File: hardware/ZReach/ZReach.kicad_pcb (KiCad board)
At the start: 4 copper layers, 120 x 120 mm, 54 parts, among them J1 USB_C_Receptacle_USB2.0, J2 Conn_02x05_Odd_Even, J3 SMA, J4 NM, J5 Qwiic_RA, J6 Conn_01x02, J7 Conn_01x05, J8 Conn_01x05, SW1 PTS810, U1 CP2102N-Axx-xQFN20, U2 EFR32xG23-QFN48, U3 AP2127K-3.3, Y1 39MHz 10ppm, Y2 32768Hz

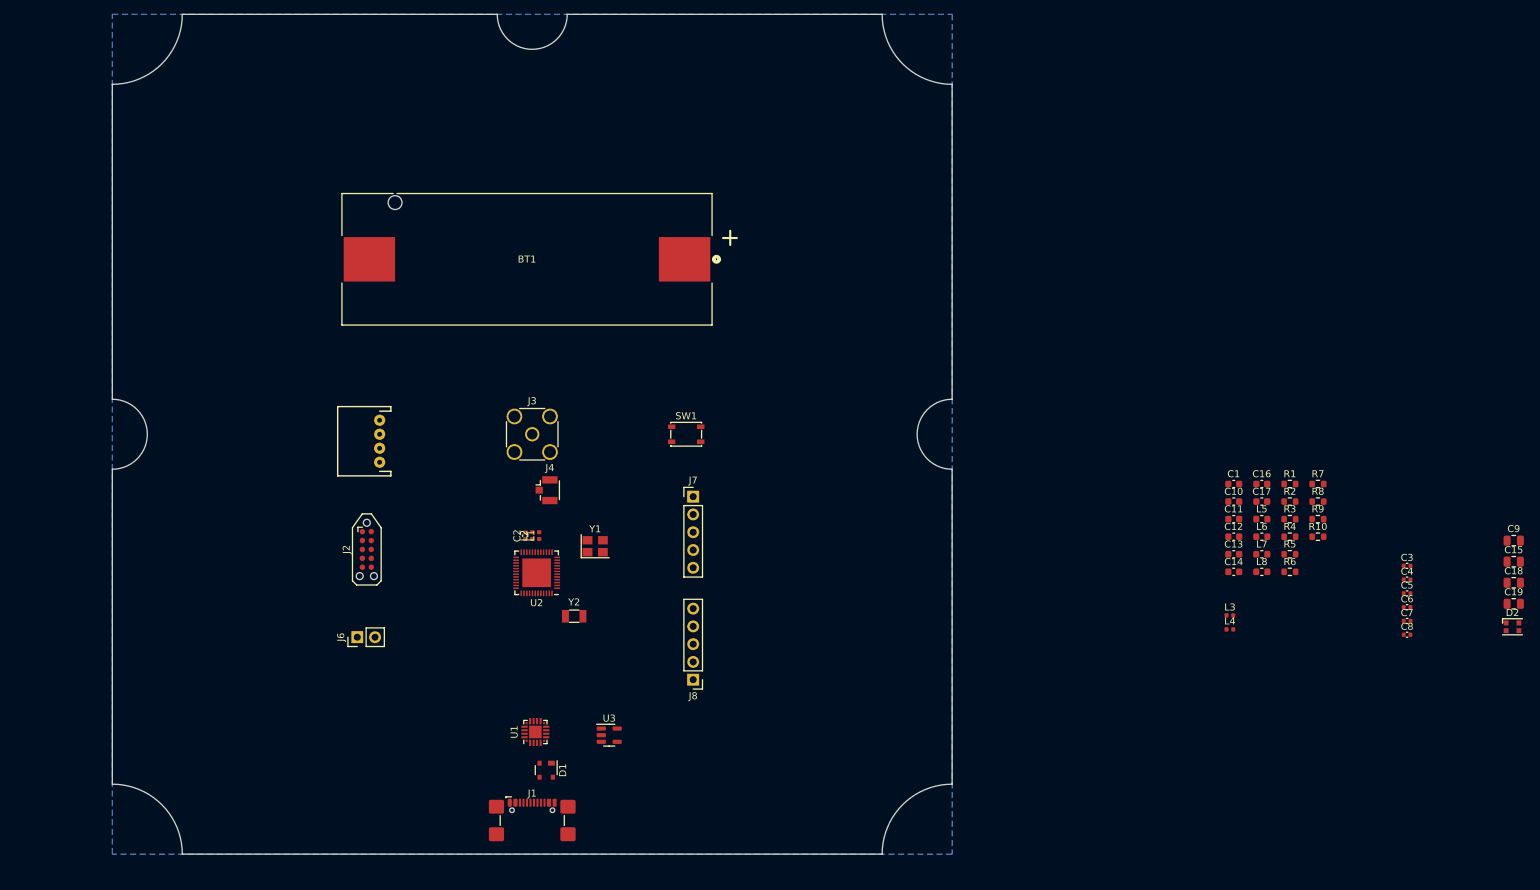
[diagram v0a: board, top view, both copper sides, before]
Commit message: PCB Layout DRC clean but needs more cleanup
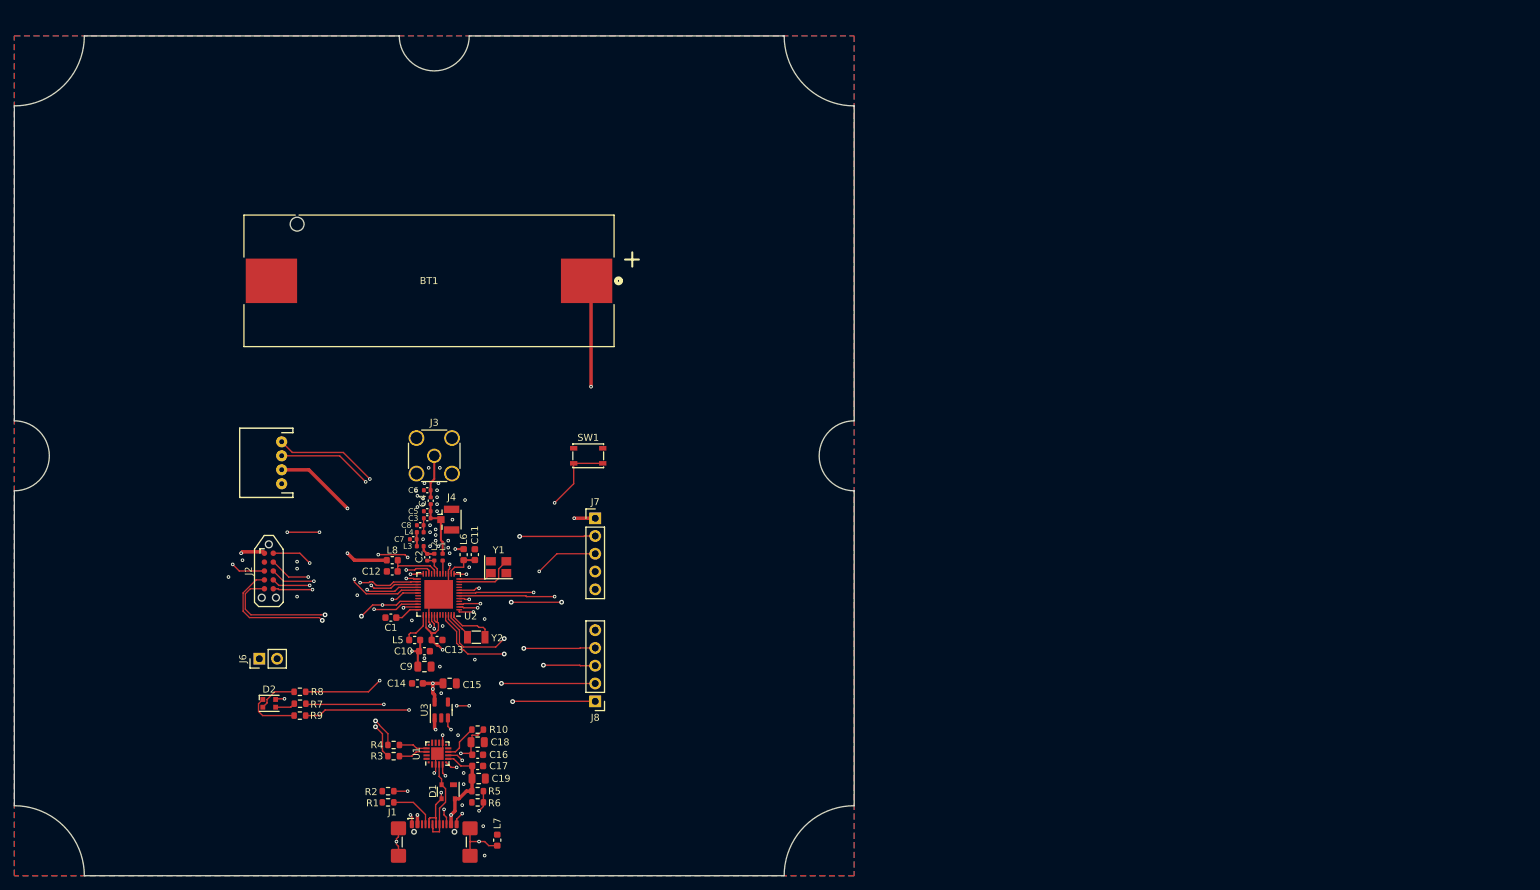
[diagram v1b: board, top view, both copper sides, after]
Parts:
- moved D2 178.0 mm to (177.4, 123.5)
- moved C9 156.7 mm to (199.6, 118.2), turned to 180 degrees
- moved C15 153.0 mm to (203.2, 120.6), turned to 180 degrees
- moved C19 150.0 mm to (207.3, 134.2), turned to 180 degrees
- moved C18 149.8 mm to (207.2, 129.0), turned to 180 degrees
- moved R7 148.8 mm to (181.8, 123.5)
- moved R9 148.2 mm to (181.8, 125.2)
- moved R8 148.0 mm to (181.8, 121.8)
- moved C7 142.5 mm to (198.0, 100.0), turned to 180 degrees
- moved C8 141.9 mm to (199.0, 98.0), turned to 180 degrees
- moved C6 141.0 mm to (200.0, 93.0)
- moved C5 140.5 mm to (200.0, 96.0)
- moved C3 140.2 mm to (200.0, 97.0)
- moved C4 140.0 mm to (200.5, 94.5), turned to 90 degrees
- moved R1 136.7 mm to (194.4, 137.6), turned to 180 degrees
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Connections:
- J7 pad 1: /PB03 -> +3.3V
- U2 pad 21: /PB03 -> unconnected-(U2-PB03-Pad21)
- U2 pad 23: /LED_RED -> unconnected-(U2-PB01-Pad23)
- U2 pad 35: unconnected-(U2-PA10-Pad35) -> /LED_RED
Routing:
- net +3.3V: track 0.00 -> 173.3 mm, vias 0 -> 9
- net /VCOMRX: track 0.00 -> 54.0 mm, vias 0 -> 3
- net /VCOMTX: track 0.00 -> 52.5 mm, vias 0 -> 4
- net /~{RESET}: track 0.00 -> 46.1 mm, vias 0 -> 6
- net /LED_BLUE: track 0.00 -> 40.6 mm, vias 0 -> 4
- net /VBUS_5V: track 0.00 -> 38.3 mm, vias 0 -> 4
- net /~{LEARN}: track 0.00 -> 38.0 mm, vias 0 -> 2
- net /I2CSCL: track 0.00 -> 32.7 mm, vias 0 -> 2
- net /I2CSDA: track 0.00 -> 32.5 mm, vias 0 -> 2
- net /PD02: track 0.00 -> 32.0 mm, vias 0 -> 3
- net /PC01: track 0.00 -> 30.0 mm, vias 0 -> 2
- net /LED_GREEN: track 0.00 -> 29.1 mm, vias 0 -> 2
- net /PC02: track 0.00 -> 29.1 mm, vias 0 -> 2
- net /PC06: track 0.00 -> 29.1 mm, vias 0 -> 2
- net /LED_RED: track 0.00 -> 28.3 mm, vias 0 -> 2
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- added copper zone on F.Cu, net GND
- added copper zone on In1.Cu, net GND
- added copper zone on In2.Cu, net GND
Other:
- rule pad_to_mask_clearance: 0 -> 0.0508
- board text added: "NOTES - UNLESS OTHERWISE SPECIFIED: FABRICATE TO MEET OR EXCEED THE REQUIREMENTS OF IPC-6012 FOR CLASS 2 AS DEFINED IN IPC-6011. MINIMUM TRACE WIDTH .008, MINIMUM CLEARANCE .008 mil MATERIAL: LAMINATE FLAME RETARDANT EPOXY-GLASS PER IPC-4101/126, 170 DEGREE C MINIMUM Tg, DECOMPOSITION TEMPERATURE 340 DEGREES C MINIMUM, T288 DELAMINATION TIME OF 35 MINUTES MINIMUM, MAXIMUM THICKNESS EXPANSION OF 3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"

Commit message: Rev A PCB released for fabrication
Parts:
- added Fid1: Fiducial_0.5mm_Mask1mm, Fiducial:Fiducial_0.5mm_Mask1mm, F.Cu at (223.0, 145.2)
- added Fid2: Fiducial_0.5mm_Mask1mm, Fiducial:Fiducial_0.5mm_Mask1mm, F.Cu at (174.4, 74.6)
- added QWIICLOGO: LOGO, ZReach:QWIIC, F.Cu at (170.4, 88.8)
- added ZWA: LOGO, ZReach:ZWA_Logo, F.Cu at (174.2, 138.8)
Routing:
- net +3.3V: track 173.3 -> 172.6 mm
- net GND: vias 52 -> 186
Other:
- board text added: "+3.3V"
- board text added: "GND"
- board text added: "INCLUDE"
- board text added: "LAYER STACKUP File Name Silkscreen TOP *.GTO Solder Mask TOP *.GTS 1 Signal Layer TOP 1.0 OZ Cu *.GTL prepreg - 0.008{dblquote} +/-.001{dblquote} 2 Signal Layer L1 1.0 OZ Cu *.G2 CORE - 0.039{dblquote} +/-.004{dblquote} 3 Signal Layer L2 1.0 OZ Cu *.G3 prepreg - 0.008{dblquote} +/-.001{dblquote} 4 Signal Layer BOT 1.0 OZ Cu *.GBL Solder Mask BOT *.GBS Silkscreen Bottom *.GBO Stencil TOP *.GTP Edg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"
- board text added: "PC00"
- board text added: "PC01"
- board text added: "PC02"
- board text added: "PC06"
- board text added: "PC07"
- board text added: "PD02"
- board text added: "PD03"
- board text added: "Z-Reach Z-Wave Controller Reference Design Revision A"

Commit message: Rev B PCB release
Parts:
- added SW2: PTS810, Button_Switch_SMD:SW_SPST_PTS810, F.Cu at (182.0, 96.5)
- C2: renamed from C12; footprint Capacitor_SMD:C_0603_1608Metric -> Capacitor_SMD:C_0402_1005Metric
- C3: renamed from C11; footprint Capacitor_SMD:C_0603_1608Metric -> Capacitor_SMD:C_0402_1005Metric
- D1: renamed from D2; value LED_BGRK -> QLSP14RGB_B; footprint LED_SMD:LED_WS2812B-2020_PLCC4_2.0x2.0mm -> ZReach:LED_QLSP14RGB
- J1: renamed from J5; footprint ZReach:JST_PTH-4 -> Connector_JST:JST_SH_SM04B-SRSS-TB_1x04-1MP_P1.00mm_Horizontal
- J2: renamed from J3; value SMA -> Conn_Coaxial
- J4: value NM -> Conn_Coaxial
- J8: renamed from J1; value USB_C_Receptacle_USB2.0 -> USB_C_Receptacle_USB2.0_16P
- U1: renamed from U2; value EFR32xG23-QFN48 -> EFR32xG23xxxxF512xM48; footprint Package_DFN_QFN:VQFN-48-1EP_6x6mm_P0.4mm_EP4.1x4.1mm -> Package_DFN_QFN:QFN-48-1EP_6x6mm_P0.4mm_EP4.3x4.3mm
- U3: renamed from U1; value CP2102N-Axx-xQFN20 -> CP2102N-Axx-xQFN24; footprint Package_DFN_QFN:SiliconLabs_QFN-20-1EP_3x3mm_P0.5mm_EP1.8x1.8mm -> Package_DFN_QFN:QFN-24-1EP_4x4mm_P0.5mm_EP2.6x2.6mm
- moved J1 3.43 mm to (175.8, 88.6), turned to -90 degrees
- moved R2 2.03 mm to (181.5, 121.5)
- moved R3 1.73 mm to (181.5, 123.5)
- moved D2 0.50 mm to (202.5, 136.1)
- moved U3 0.47 mm to (201.0, 130.5)
- moved R1 0.30 mm to (181.5, 125.2)
- moved L6 0.20 mm to (202.4, 102.6)
- moved C3 0.20 mm to (206.8, 102.4)
- moved C2 0.20 mm to (195.2, 104.6)
- turned Y1 to 180 degrees
- renumbered C5 to C1, C6 to C10, C14 to C11, C15 to C12, C18 to C13, C19 to C14, C13 to C15, C17 to C16, C9 to C17, C10 to C18, C16 to C19, C8 to C5, C1 to C6, C3 to C7, C7 to C8, C2 to C9, D1 to D2, Fid2 to Fid1, Fid1 to Fid2, J2 to J3, J7 to J5, J8 to J7, L8 to L1, L3 to L2, L4 to L3, L2 to L4, L6 to L5, L1 to L6, L5 to L7, L7 to L8, R9 to R1, R1 to R10, R7 to R2, R8 to R3, R3 to R4, R4 to R5, R5 to R7, R2 to R8, R10 to R9, U3 to U2, Y2 to Y1, Y1 to Y2
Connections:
- C13 pad 2: Net-(U1-VDD) -> Net-(U3-VDD)
- C19 pad 2: Net-(U1-VDD) -> Net-(U3-VDD)
- D1 pad 1: Net-(D2-BA) -> Net-(D1-GK)
- D1 pad 2: Net-(D2-GA) -> Net-(D1-RK)
- D1 pad 3: Net-(D2-RA) -> +3.3V
- D1 pad 4: +3.3V -> Net-(D1-BK)
- R1 pad 1: Net-(D2-BA) -> Net-(D1-RK)
- R2 pad 1: Net-(D2-RA) -> Net-(D1-BK)
- R3 pad 1: Net-(D2-GA) -> Net-(D1-GK)
- R4 pad 1: Net-(U1-TXD) -> Net-(U3-TXD)
- R5 pad 1: Net-(U1-RXD) -> Net-(U3-RXD)
- R9 pad 2: Net-(U1-VDD) -> Net-(U3-VDD)
- U1 pad 29: /TD1 -> /TCLK
- U1 pad 30: /TCLK -> /TD1
- U1 pad 47: Net-(U2-PD01_LFXI) -> Net-(U1-PD01_LFXI)
- U1 pad 48: Net-(U2-PD00_LFXO) -> Net-(U1-PD00_LFXO)
- U3 pad 12: GND -> unconnected-(U3-RS485/GPIO.2-Pad12)
- U3 pad 17: Net-(U1-RXD) -> unconnected-(U3-SUSPEND-Pad17)
- U3 pad 18: Net-(U1-TXD) -> unconnected-(U3-~{CTS}-Pad18)
- U3 pad 2: unconnected-(U1-CLK/GPIO.0-Pad2) -> GND
- U3 pad 20: unconnected-(U1-~{TXT}/GPIO.2-Pad20) -> Net-(U3-RXD)
- U3 pad 21: GND -> Net-(U3-TXD)
- U3 pad 3: GND -> /DPLUS
- U3 pad 4: /DPLUS -> /DMINUS
- U3 pad 5: /DMINUS -> Net-(U3-VDD)
- U3 pad 6: Net-(U1-VDD) -> Net-(U3-VDD)
- Y1 pad 1: Net-(U2-PD00_LFXO) -> Net-(U1-PD01_LFXI)
- Y1 pad 2: Net-(U2-PD01_LFXI) -> Net-(U1-PD00_LFXO)
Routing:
- net Net-(U3-VDD): track 0.00 -> 13.1 mm, vias 0 -> 2
- net Net-(U1-VDD): track 10.6 -> 0.00 mm, vias 2 -> 0
- net +3.3V: track 172.6 -> 180.1 mm
- net Net-(D2-BA): track 7.29 -> 0.00 mm
- net Net-(U2-PD00_LFXO): track 6.61 -> 0.00 mm
- net Net-(U1-PD00_LFXO): track 0.00 -> 6.61 mm
- net Net-(D2-GA): track 5.67 -> 0.00 mm
- net Net-(D1-RK): track 0.00 -> 4.90 mm
- net Net-(U2-PD01_LFXI): track 4.17 -> 0.00 mm
- net Net-(U1-PD01_LFXI): track 0.00 -> 4.17 mm
- net Net-(U1-TXD): track 4.13 -> 0.00 mm
- net Net-(U1-RXD): track 4.07 -> 0.00 mm
- net /LED_GREEN: track 29.1 -> 32.8 mm
- net Net-(U3-TXD): track 0.00 -> 3.35 mm
- net Net-(U3-RXD): track 0.00 -> 3.18 mm
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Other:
- board text added: "3V3"
- board text added: "RST"
- board text added: "RX"
- board text added: "SWCLK"
- board text added: "SWDIO"
- board text added: "SWO"
- board text added: "TCLK"
- board text added: "TD1"
- board text added: "TX"
- board text added: "Z-Reach Z-Wave Controller Reference Design Revision B"
- board text removed: "Z-Reach Z-Wave Controller Reference Design Revision A"
